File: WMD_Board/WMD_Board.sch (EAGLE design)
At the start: 69 parts, among them IC1 FGPMMOPA6H, J1 EMPCB.SMAFSTJ.B.HT, J2 5015680607, Q1 SI2323DS-T1-E3, Q2 SI2323DS-T1-E3, Q3 SI2312BDS, U1 STM32L053C8T6, U2 BSS138, U3 RFM69HCW, U4 BSS138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

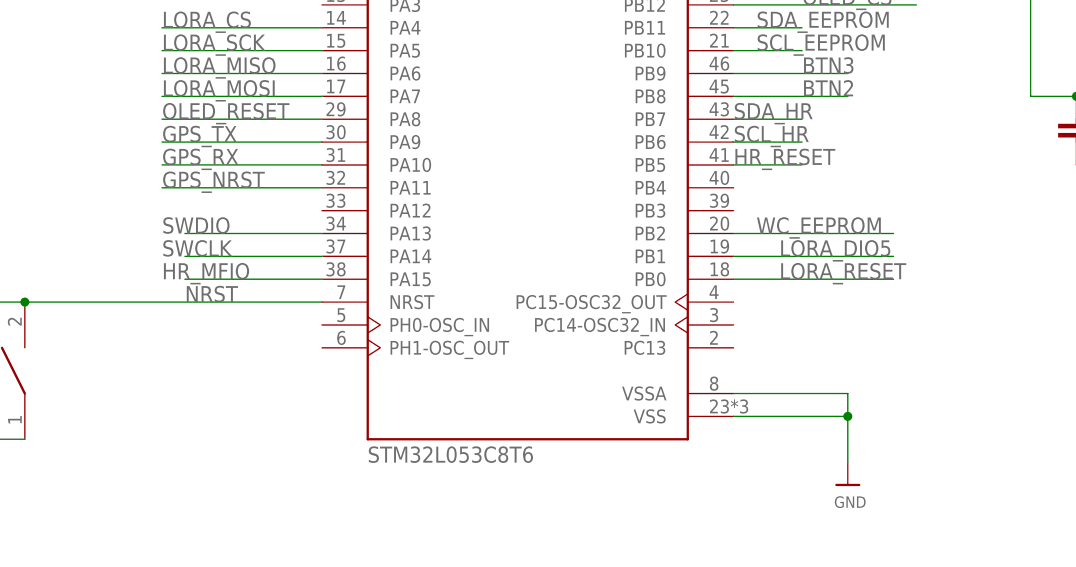
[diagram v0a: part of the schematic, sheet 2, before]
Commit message: Routed MFIO Pin (routing completed)
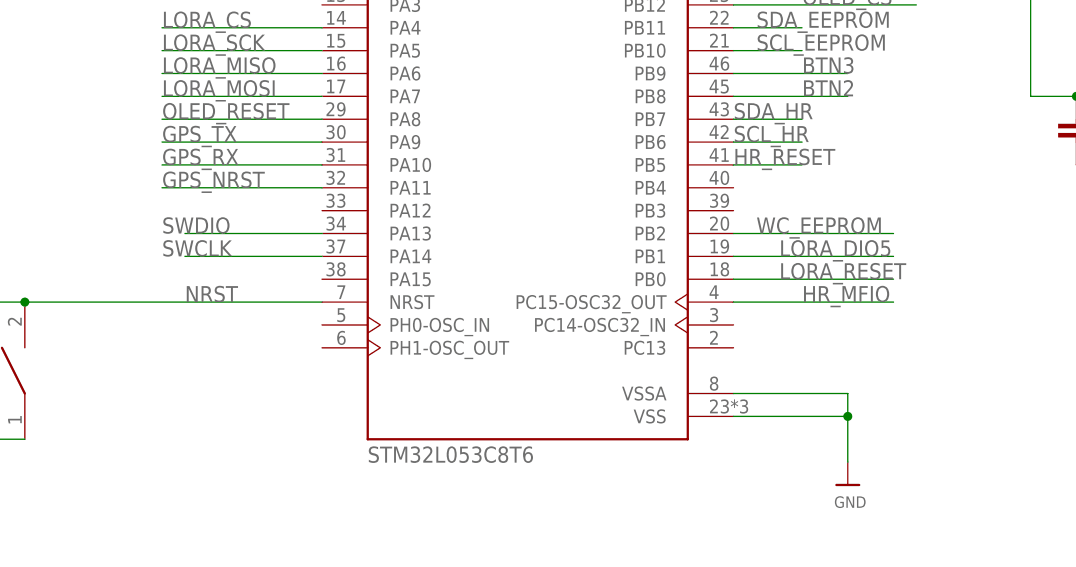
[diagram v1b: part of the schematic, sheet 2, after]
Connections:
- net HR_MFIO: now also U1.PC15-OSC32_OUT; no longer U1.PA15
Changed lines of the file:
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@@
 <net name="HR_MFIO" class="0">
 <segment>
-<pinref part="U1" gate="G$1" pin="PA15"/>
-<wire x1="76.2" y1="185.42" x2="60.96" y2="185.42" width="0.1524" layer="91"/>
-<label x="58.42" y="185.42" size="1.778" layer="95"/>
+<pinref part="U1" gate="G$1" pin="PC15-OSC32_OUT"/>
+<wire x1="121.92" y1="182.88" x2="139.7" y2="182.88" width="0.1524" layer="91"/>
+<label x="129.54" y="182.88" size="1.778" layer="95"/>
 </segment>
 </net>

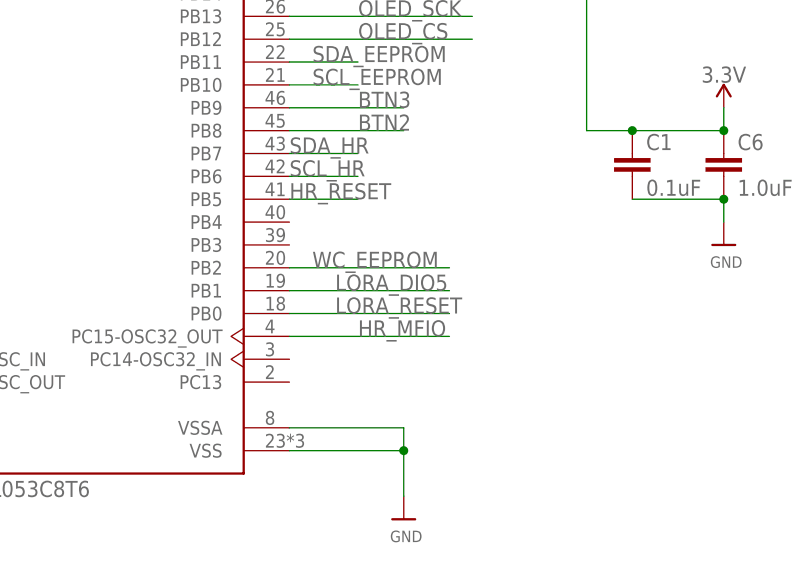
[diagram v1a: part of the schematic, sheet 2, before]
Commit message: hole spacing
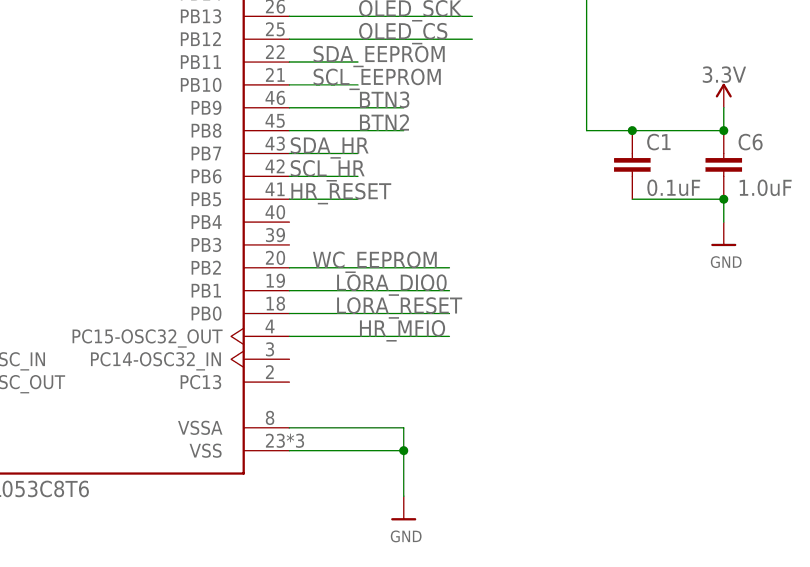
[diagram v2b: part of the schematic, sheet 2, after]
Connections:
- removed net DIO0: U3.DIO0
- new net LORA_DIO0: U1.PB1, U3.DIO0
- net LORA_DIO5: no longer U1.PB1
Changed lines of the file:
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@@
-</segment>
-</net>
-<net name="LORA_DIO5" class="0">
-<segment>
-<pinref part="U1" gate="G$1" pin="PB1"/>
-<wire x1="121.92" y1="187.96" x2="139.7" y2="187.96" width="0.1524" layer="91"/>
-<label x="127" y="187.96" size="1.778" layer="95"/>
 </segment>
 </net>
@@
 <wire x1="121.92" y1="182.88" x2="139.7" y2="182.88" width="0.1524" layer="91"/>
 <label x="129.54" y="182.88" size="1.778" layer="95"/>
+</segment>
+</net>
+<net name="LORA_DIO0" class="0">
+<segment>
+<pinref part="U1" gate="G$1" pin="PB1"/>
+<wire x1="121.92" y1="187.96" x2="139.7" y2="187.96" width="0.1524" layer="91"/>
+<label x="127" y="187.96" size="1.778" layer="95"/>
 </segment>
 </net>
@@
 </segment>
 </net>
-<net name="DIO0" class="0">
+<net name="LORA_DIO0" class="0">
 <segment>
 <wire x1="81.28" y1="220.98" x2="66.04" y2="220.98" width="0.1524" layer="91"/>

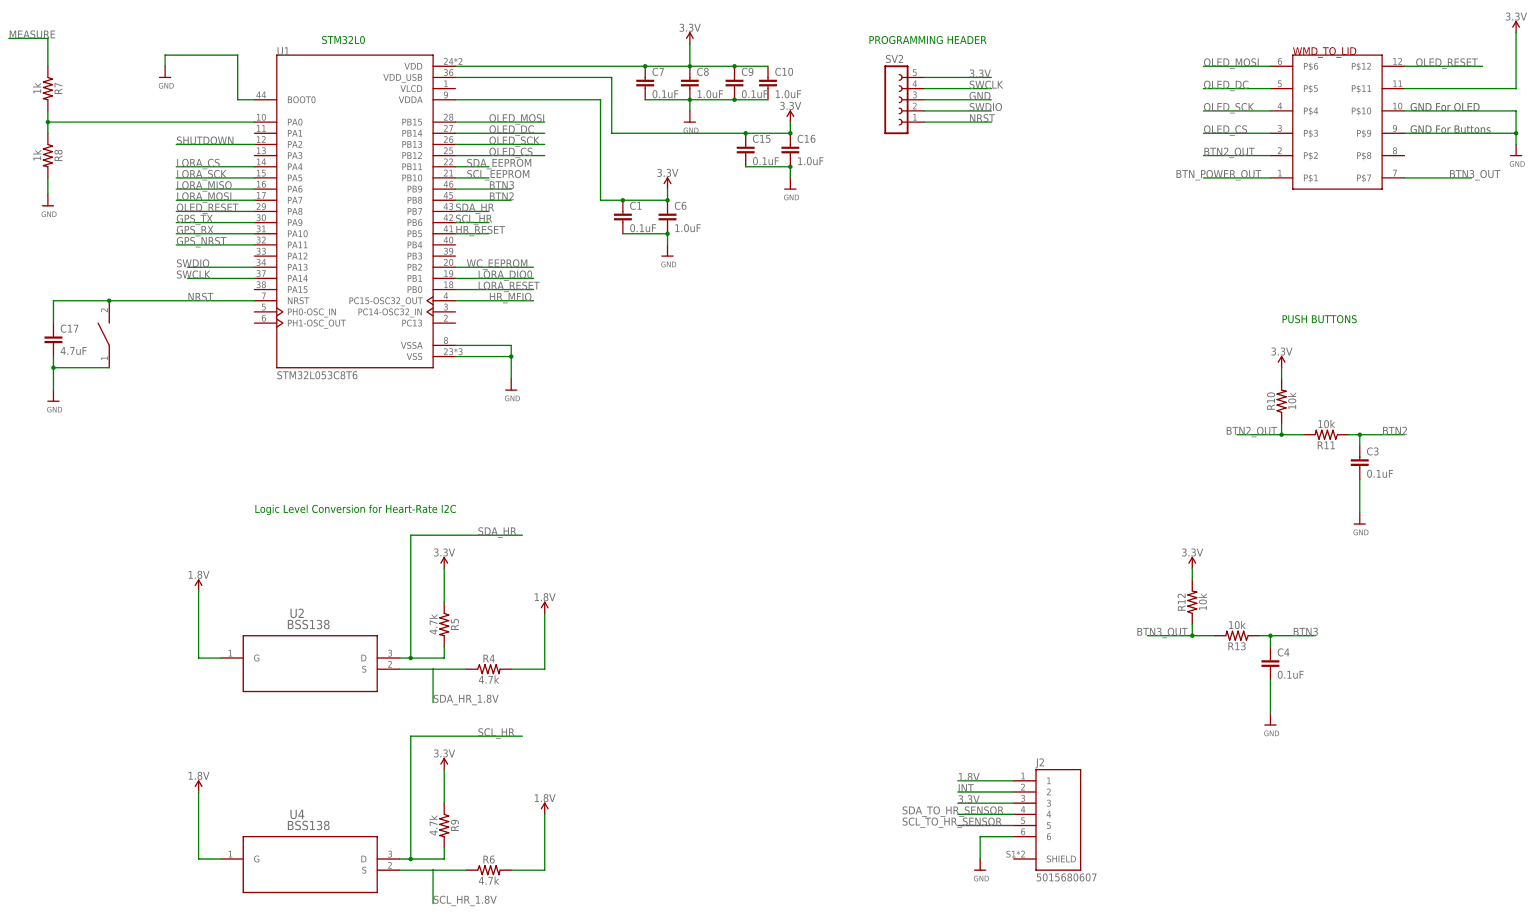
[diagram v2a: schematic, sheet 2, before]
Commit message: added heartbeat led, ferrite bead, pin breakout
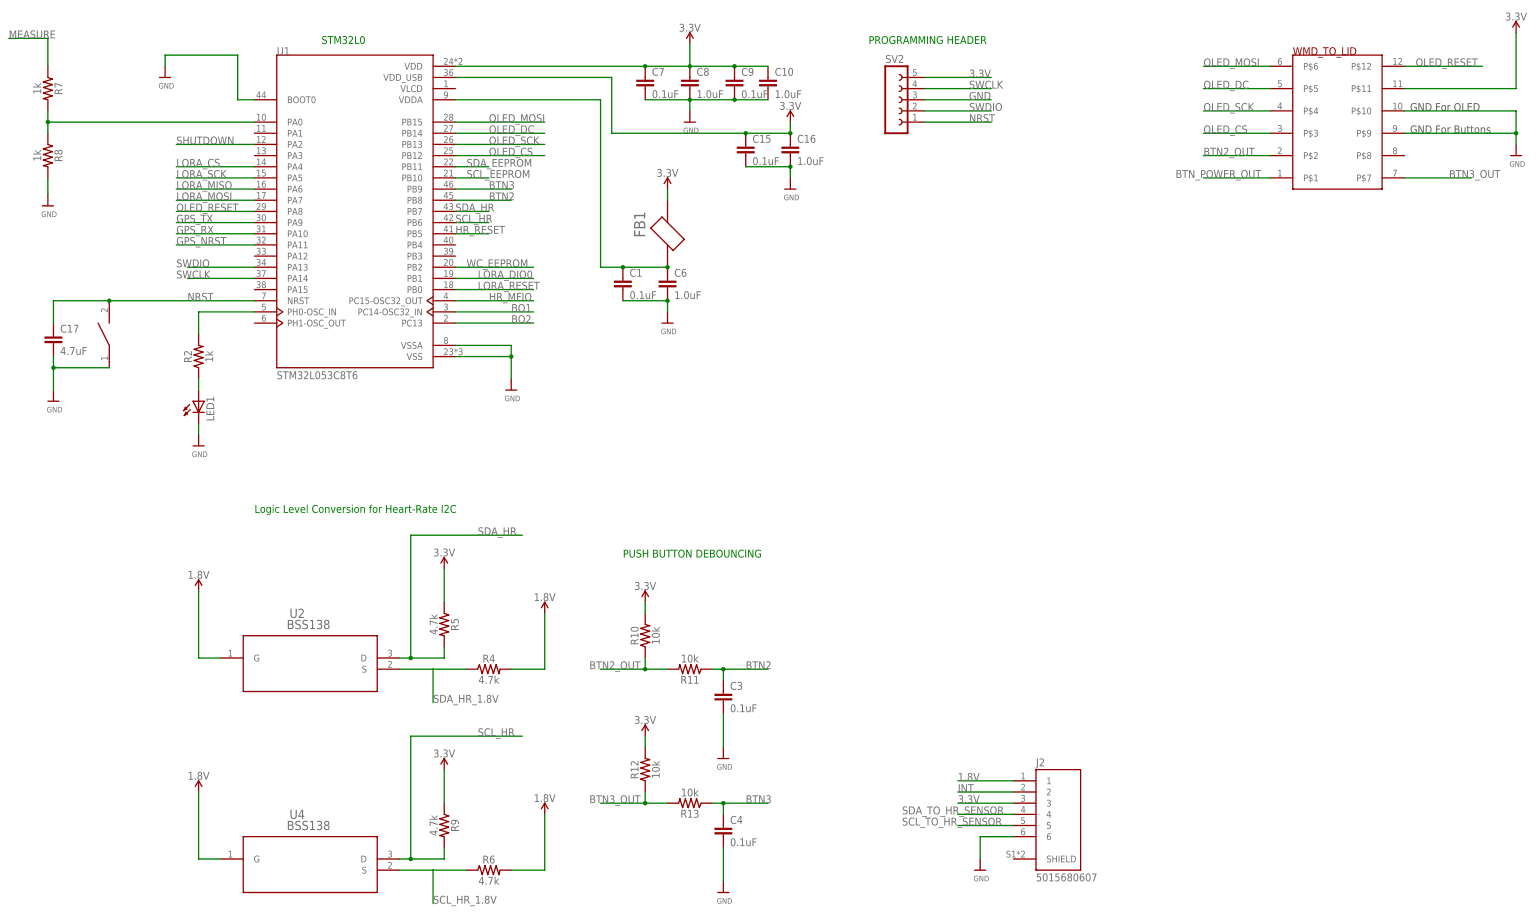
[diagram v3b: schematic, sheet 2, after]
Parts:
- added FB1: FERRITE_BEAD, Ferrite_Bead:FERRITE_BEAD
- added LED1: (no value), led:LEDCHIP-LED0805
- added R2: 1k, SparkFun-Resistors:1KOHM-0603-1/10W-1%
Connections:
- new net BO1: U1.PC14-OSC32_IN
- new net BO2: U1.PC13
- new net N$1: LED1.A, R2.1
- new net N$12: R2.2, U1.PH0-OSC_IN
- new net N$5: C1.1, C6.1, FB1.2, U1.VDDA
- net 3.3V: now also FB1.1; no longer C1.1, C6.1, U1.VDDA
- net GND: now also LED1.C
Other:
- note added: "PUSH BUTTON DEBOUNCING"
- note removed: "PUSH BUTTONS"
- moved on the sheet: C1, C3, C4, C6, R10, R11, R12, R13

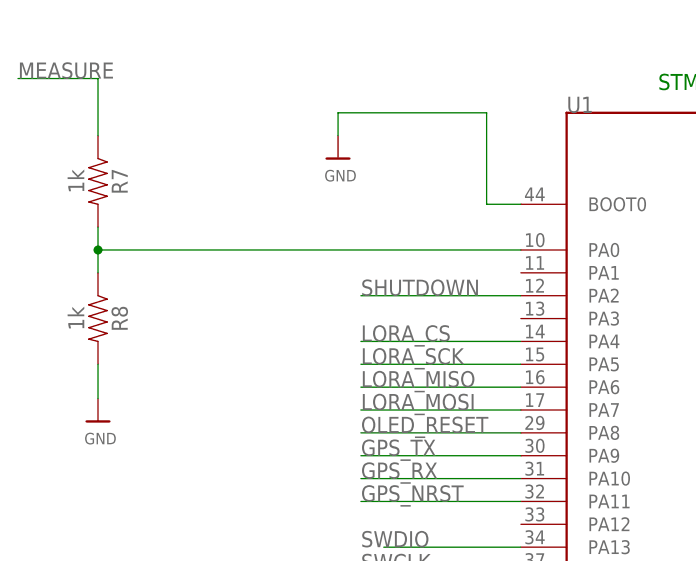
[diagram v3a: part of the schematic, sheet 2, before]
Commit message: made changes besides zener diode
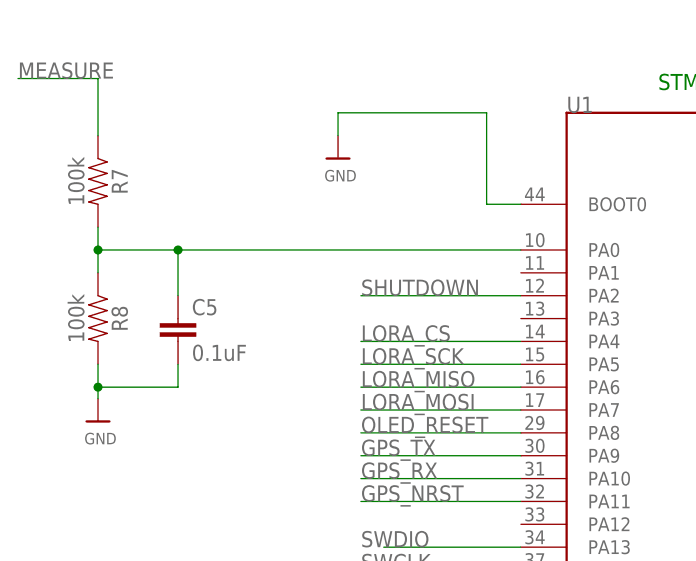
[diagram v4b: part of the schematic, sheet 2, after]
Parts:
- added C5: 0.1uF, SparkFun-Capacitors:0.1UF-0603-25V-(+80/-20%)
- R1, R18: value 1k -> 4.7k
- R17: value 1k -> 10k
- R19, R20, R7, R8: value 1k -> 100k
- R21: value 1k -> 300k
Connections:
- net GND: now also C5.2
- net N$4: now also C5.1
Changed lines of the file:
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@@
 <setting verticaltext="up"/>
 </settings>
-<grid distance="0.1" unitdist="inch" unit="inch" style="lines" multiple="1" display="no" altdistance="0.01" altunitdist="inch" altunit="inch"/>
+<grid distance="0.05" unitdist="inch" unit="inch" style="lines" multiple="1" display="no" altdistance="0.01" altunitdist="inch" altunit="inch"/>
 <layers>
 <layer number="1" name="Top" color="4" fill="1" visible="no" active="no"/>
@@
 <part name="U$28" library="microbuilder" deviceset="GND" device=""/>
 <part name="U$29" library="microbuilder" deviceset="GND" device=""/>
-<part name="R1" library="SparkFun-Resistors" deviceset="1KOHM" device="-0603-1/10W-1%" value="1k"/>
-<part name="R18" library="SparkFun-Resistors" deviceset="1KOHM" device="-0603-1/10W-1%" value="1k"/>
+<part name="R1" library="SparkFun-Resistors" deviceset="1KOHM" device="-0603-1/10W-1%" value="4.7k"/>
+<part name="R18" library="SparkFun-Resistors" deviceset="1KOHM" device="-0603-1/10W-1%" value="4.7k"/>
 <part name="SUPPLY26" library="SparkFun-PowerSymbols" deviceset="3.3V" device=""/>
 <part name="SUPPLY27" library="SparkFun-PowerSymbols" deviceset="3.3V" device=""/>
@@
 <part name="U$35" library="microbuilder" deviceset="GND" device=""/>
 <part name="U$5" library="microbuilder" deviceset="GND" device=""/>
-<part name="R7" library="SparkFun-Resistors" deviceset="1KOHM" device="-0603-1/10W-1%" value="1k"/>
-<part name="R8" library="SparkFun-Resistors" deviceset="1KOHM" device="-0603-1/10W-1%" value="1k"/>
+<part name="R7" library="SparkFun-Resistors" deviceset="1KOHM" device="-0603-1/10W-1%" value="100k"/>
+<part name="R8" library="SparkFun-Resistors" deviceset="1KOHM" device="-0603-1/10W-1%" value="100k"/>
 <part name="U$36" library="microbuilder" deviceset="GND" device=""/>
 <part name="U$38" library="TS4148_RY" deviceset="TS4148C_RZG" device=""/>
-<part name="R17" library="SparkFun-Resistors" deviceset="1KOHM" device="-0603-1/10W-1%" value="1k"/>
-<part name="R19" library="SparkFun-Resistors" deviceset="1KOHM" device="-0603-1/10W-1%" value="1k"/>
-<part name="R20" library="SparkFun-Resistors" deviceset="1KOHM" device="-0603-1/10W-1%" value="1k"/>
-<part name="R21" library="SparkFun-Resistors" deviceset="1KOHM" device="-0603-1/10W-1%" value="1k"/>
+<part name="R17" library="SparkFun-Resistors" deviceset="1KOHM" device="-0603-1/10W-1%" value="10k"/>
+<part name="R19" library="SparkFun-Resistors" deviceset="1KOHM" device="-0603-1/10W-1%" value="100k"/>
+<part name="R20" library="SparkFun-Resistors" deviceset="1KOHM" device="-0603-1/10W-1%" value="100k"/>
+<part name="R21" library="SparkFun-Resistors" deviceset="1KOHM" device="-0603-1/10W-1%" value="300k"/>
 <part name="C2" library="SparkFun-Capacitors" deviceset="1.0UF" device="-0603-16V-10%" value="1.0uF"/>
 <part name="C27" library="SparkFun-Capacitors" deviceset="1.0UF" device="-0603-16V-10%" value="1.0uF"/>
@@
 <part name="R2" library="SparkFun-Resistors" library_urn="urn:adsk.eagle:library:532" deviceset="1KOHM" device="-0603-1/10W-1%" package3d_urn="urn:adsk.eagle:package:39650/1" value="1k"/>
 <part name="U$1" library="microbuilder" deviceset="GND" device=""/>
+<part name="C5" library="SparkFun-Capacitors" deviceset="0.1UF" device="-0603-25V-(+80/-20%)" value="0.1uF"/>
 </parts>
 <sheets>
@@
 <attribute name="VALUE" x="61.976" y="147.32" size="1.27" layer="96"/>
 </instance>
+<instance part="C5" gate="G$1" x="38.1" y="213.36" smashed="yes">
+<attribute name="NAME" x="39.624" y="216.281" size="1.778" layer="95" font="vector"/>
+<attribute name="VALUE" x="39.624" y="211.201" size="1.778" layer="96" font="vector"/>
+</instance>
 </instances>
 <busses>
@@
 <pinref part="U$36" gate="G$1" pin="GND"/>
 <pinref part="R8" gate="G$1" pin="2"/>
-<wire x1="29.21" y1="207.01" x2="29.21" y2="210.82" width="0.1524" layer="91"/>
+<wire x1="29.21" y1="207.01" x2="29.21" y2="208.28" width="0.1524" layer="91"/>
+<pinref part="C5" gate="G$1" pin="2"/>
+<wire x1="29.21" y1="208.28" x2="29.21" y2="210.82" width="0.1524" layer="91"/>
+<wire x1="38.1" y1="210.82" x2="38.1" y2="208.28" width="0.1524" layer="91"/>
+<wire x1="38.1" y1="208.28" x2="29.21" y2="208.28" width="0.1524" layer="91"/>
+<junction x="29.21" y="208.28"/>
 </segment>
 <segment>
@@
 <segment>
 <pinref part="U1" gate="G$1" pin="PA0"/>
-<wire x1="76.2" y1="223.52" x2="29.21" y2="223.52" width="0.1524" layer="91"/>
+<wire x1="76.2" y1="223.52" x2="38.1" y2="223.52" width="0.1524" layer="91"/>
 <pinref part="R8" gate="G$1" pin="1"/>
+<wire x1="38.1" y1="223.52" x2="29.21" y2="223.52" width="0.1524" layer="91"/>
 <wire x1="29.21" y1="223.52" x2="29.21" y2="220.98" width="0.1524" layer="91"/>
 <pinref part="R7" gate="G$1" pin="2"/>
 <wire x1="29.21" y1="226.06" x2="29.21" y2="223.52" width="0.1524" layer="91"/>
 <junction x="29.21" y="223.52"/>
-</segment>
-</net>
+<pinref part="C5" gate="G$1" pin="1"/>
+<wire x1="38.1" y1="218.44" x2="38.1" y2="223.52" width="0.1524" layer="91"/>
+<junction x="38.1" y="223.52"/>
+</segment>
+</net>
